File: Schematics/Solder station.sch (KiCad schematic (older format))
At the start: 74 parts

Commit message: Schematic cleanup
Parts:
- removed Q?: 2N3904, Package_TO_SOT_THT:TO-92_Inline, symbol Transistor_BJT:2N3904
- removed R?: 1k, symbol Device:R
- A?: value Arduino_Nano_v2.x -> Arduino
- J?: value To_airgun_HT -> Airgun_HT
- J?: value To_iron_HT -> Iron_HT
- J?: value To_airgun_FAN -> Airgun_fan
- J?: value From_iron_temp -> Iron_temp
- J?: value From_airgun_temp -> Airgun_temp
- J?: value From_airgun_SW -> Airgun_SW
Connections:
- wire segments 348 -> 344
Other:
- moved on the sheet: C?, J?, R?, SW?B, U?

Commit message: Updated electronics for the thermal couplers. Iron works now, with rough calibration.
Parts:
- removed D? (x5): D, symbol Device:D
- removed J?: Airgun_SW, symbol Connector_Generic:Conn_01x01
- removed Q? (x3): 2N3904, Package_TO_SOT_THT:TO-92_Inline, symbol Transistor_BJT:2N3904
- removed R? (x2): 100k, symbol Device:R
- removed R? (x2): 10k, symbol Device:R
- removed R? (x2): 1k, symbol Device:R
- removed RV?: 20k, symbol Device:R_POT_TRIM
- removed SW?: Mains_SW, symbol Switch:SW_DPDT_x2
- removed U?: Display, symbol DIV_custom:SSD1306
- removed U?: 4017, symbol 4xxx:4017
- added C? (x3): 0,1uF, symbol Device:C
- added J?: 24VAC, symbol Connector_Generic:Conn_01x02
- added J?: air_gn_sw, symbol Connector:Conn_01x01_Female
- added J?: main_sw, symbol Connector:Conn_01x01_Female
- added Q? (x3): TIP122, Package_TO_SOT_THT:TO-220-3_Vertical, symbol Transistor_BJT:TIP122
- added R? (x2): 1k, symbol Device:R
- added R? (x2): 10k, symbol Device:R
- added RV?: 20k, symbol Device:R_POT_TRIM
- added U?: SH1106, symbol DIV_custom:SH1106
- SW_blue: renamed from SW?; value SW_1 -> blue_sw
- SW_orag: renamed from SW?; value SW_2 -> orag_sw
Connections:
- wire segments 344 -> 302
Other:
- moved on the sheet: D?, J?, K?, Q?, R?, RV?, SW?A, U?, U?A, U?B

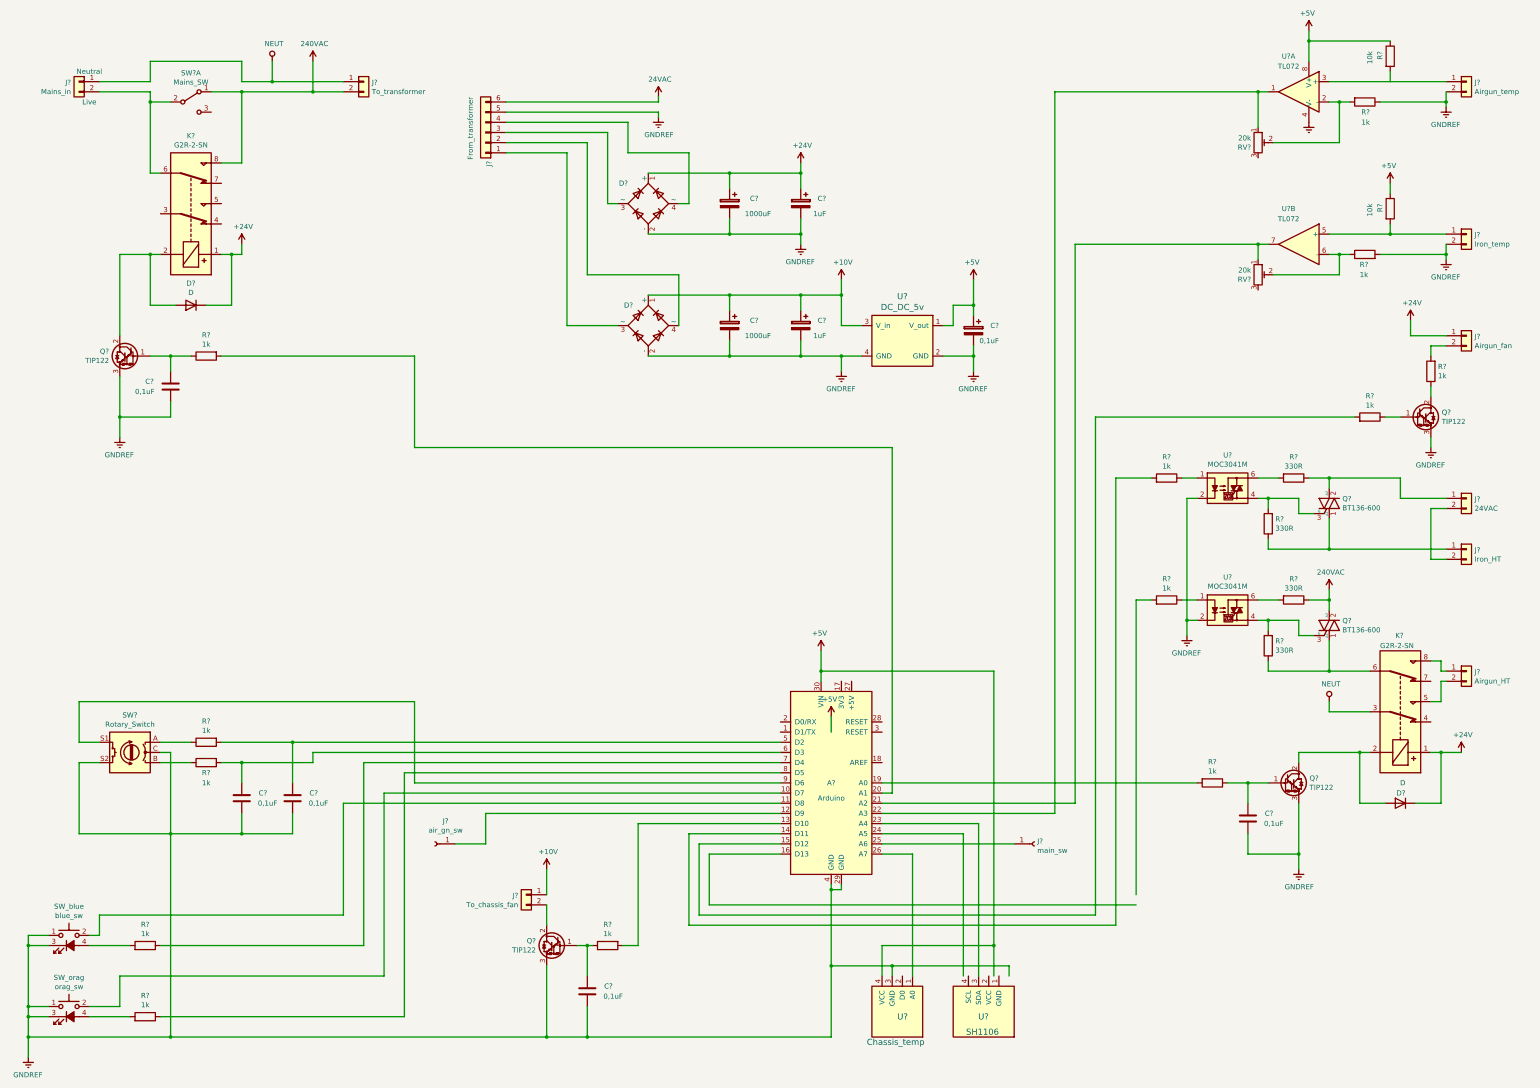
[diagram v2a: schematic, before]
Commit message: Changed electronics onto 2 seperate boards.
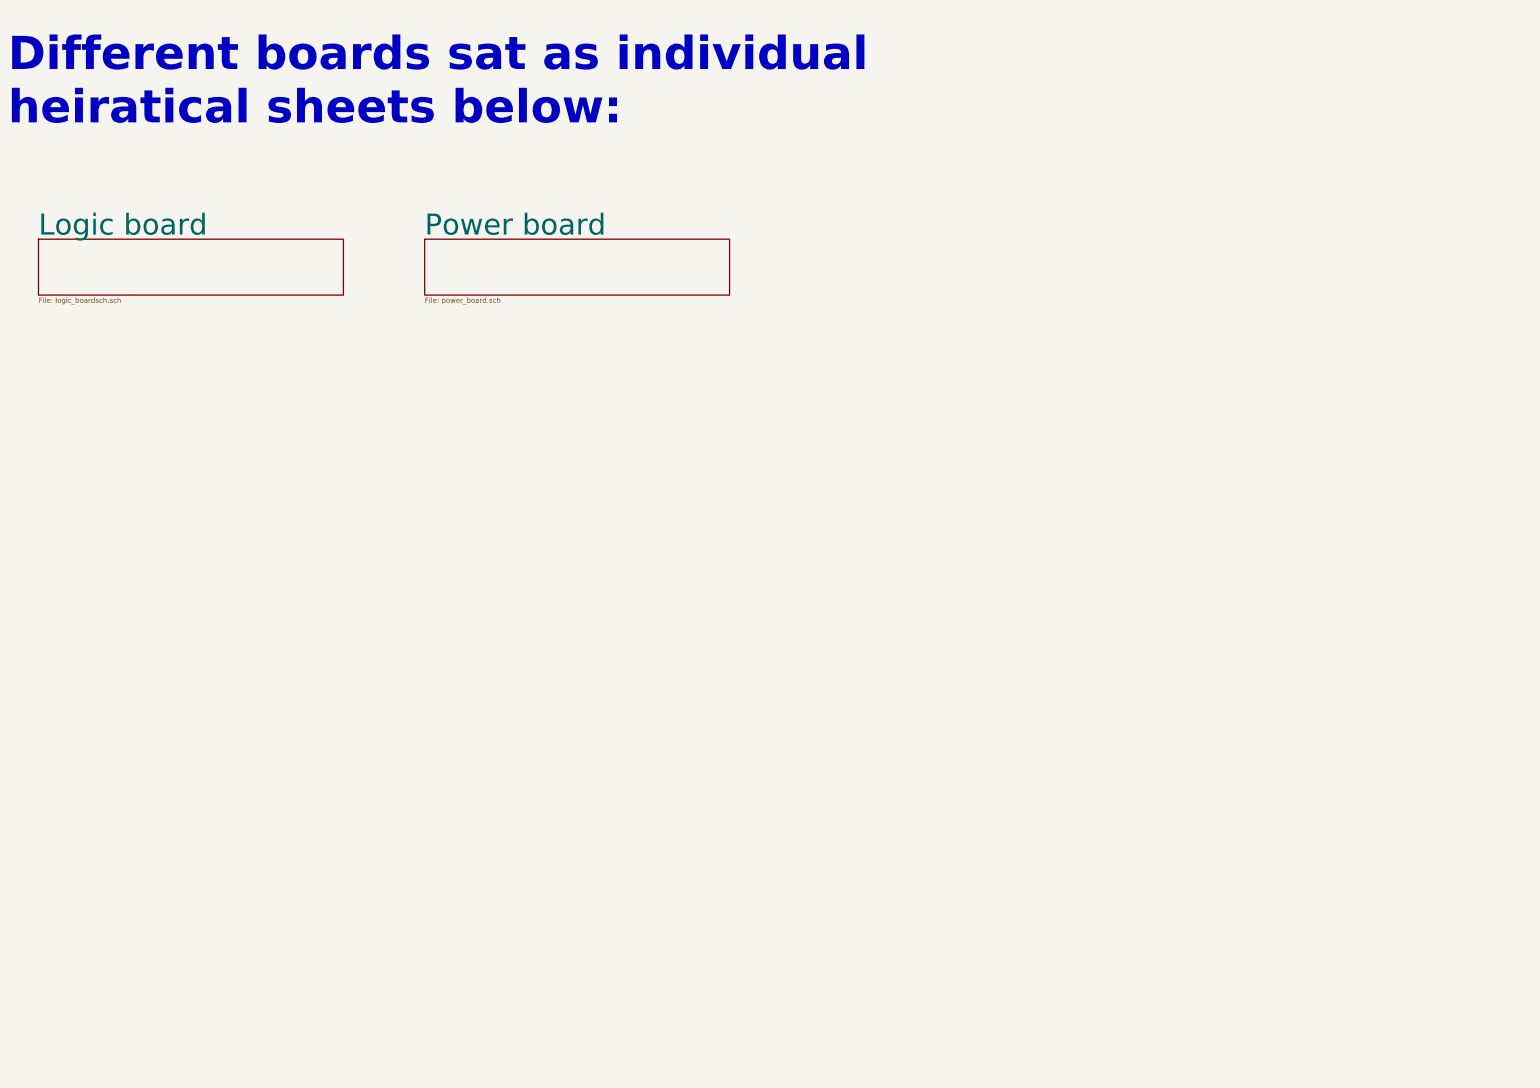
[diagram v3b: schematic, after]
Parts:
- removed A?: Arduino, Module:Arduino_Nano, symbol MCU_Module:Arduino_Nano_v2.x
- removed C? (x5): 0,1uF, symbol Device:C
- removed C? (x2): 1000uF, symbol Device:CP
- removed C? (x2): 1uF, symbol Device:CP
- removed C?: 0,1uF, symbol Device:CP
- removed D? (x2): D_Bridge_+-AA, symbol Device:D_Bridge_+-AA
- removed D? (x2): D, symbol Device:D
- removed J?: To_chassis_fan, symbol Connector_Generic:Conn_01x02
- removed J?: From_transformer, symbol Connector_Generic:Conn_01x06
- removed J?: 24VAC, symbol Connector_Generic:Conn_01x02
- removed J?: To_transformer, symbol Connector_Generic:Conn_01x02
- removed J?: Airgun_HT, symbol Connector_Generic:Conn_01x02
- removed J?: Iron_HT, symbol Connector_Generic:Conn_01x02
- removed J?: air_gn_sw, symbol Connector:Conn_01x01_Female
- removed J?: main_sw, symbol Connector:Conn_01x01_Female
- removed J?: Airgun_fan, symbol Connector_Generic:Conn_01x02
- removed J?: Iron_temp, symbol Connector_Generic:Conn_01x02
- removed J?: Airgun_temp, symbol Connector_Generic:Conn_01x02
- removed J?: Mains_in, symbol Connector_Generic:Conn_01x02
- removed K? (x2): G2R-2-SN, symbol DIV_custom:G2R-2-SN
- removed Q? (x4): TIP122, Package_TO_SOT_THT:TO-220-3_Vertical, symbol Transistor_BJT:TIP122
- removed Q? (x2): BT136-600, Package_TO_SOT_THT:TO-220-3_Vertical, symbol Triac_Thyristor:BT136-600
- removed R? (x13): 1k, symbol Device:R
- removed R? (x2): 10k, symbol Device:R
- removed R? (x4): 330R, symbol Device:R
- removed RV? (x2): 20k, symbol Device:R_POT_TRIM
- removed SW?: Rotary_Switch, symbol Device:Rotary_Encoder_Switch
- removed SW?: Mains_SW, symbol Switch:SW_DPDT_x2
- removed SW_blue: blue_sw, symbol Switch:SW_Push_LED
- removed SW_orag: orag_sw, symbol Switch:SW_Push_LED
- removed U?: Chassis_temp, symbol DIV_custom:AD_tmp_sens
- removed U?: DC_DC_5v, symbol DIV_custom:DC_DC_conv
- removed U? (x2): MOC3041M, symbol Relay_SolidState:MOC3041M
- removed U?: SH1106, symbol DIV_custom:SH1106
- removed U? (x3): TL072, symbol Amplifier_Operational:TL072
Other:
- note added: "Different boards sat as individual\nheiratical sheets below:"

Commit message: Tja
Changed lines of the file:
@@
 EESchema Schematic File Version 4
 LIBS:Solder station-cache
-LIBS:Power board-cache
 EELAYER 26 0
 EELAYER END
@@
 U 5C287C9A
 F0 "Logic board" 207
-F1 "logic_boardsch.sch" 50
+F1 "logic_board.sch" 50
 $EndSheet
 Text Notes 600  1650 0    326  ~ 65
